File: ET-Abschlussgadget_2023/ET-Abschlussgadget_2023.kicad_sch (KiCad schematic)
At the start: 12 parts, among them U1 ATtiny10-TS

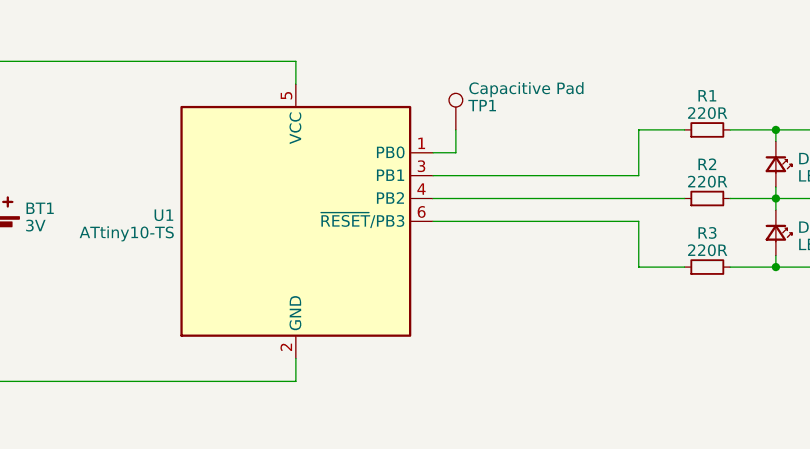
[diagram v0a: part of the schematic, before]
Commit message: Add basic layout
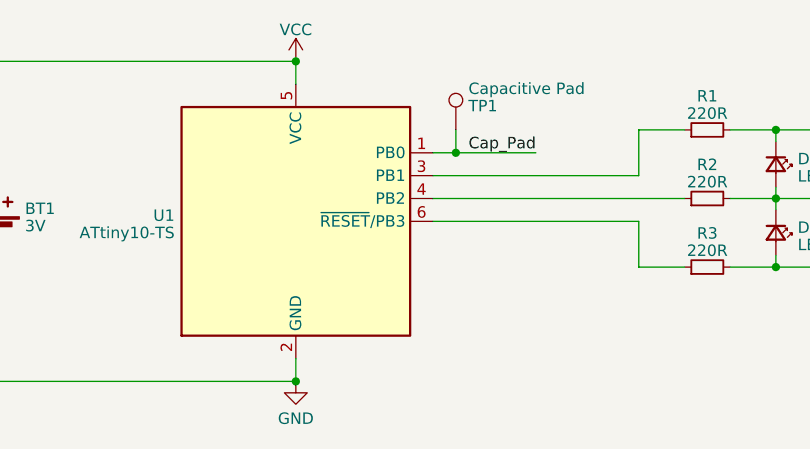
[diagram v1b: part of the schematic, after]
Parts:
- BT1: footprint (none) -> Battery:BatteryHolder_Keystone_3000_1x12mm
- D1, D2, D3, D4, D5: footprint (none) -> LED_SMD:LED_0805_2012Metric_Pad1.15x1.40mm_HandSolder
- D6: footprint (none) -> LED_SMD:LED_LiteOn_LTST-S326
- R1, R2, R3: footprint (none) -> Resistor_SMD:R_0805_2012Metric_Pad1.20x1.40mm_HandSolder
- TP1: footprint (none) -> TestPoint:TestPoint_Pad_4.0x4.0mm
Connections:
- net Cap_Pad: now reaches TP1.1, U1.1 (PB0)
- net VCC: now reaches BT1.1 (+), U1.5 (VCC)
- net GND: now reaches BT1.2 (-), U1.2 (GND)
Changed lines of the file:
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@@
 (kicad_sch (version 20230121) (generator eeschema)
   (paper "A4")
+  (junction (at 106.68 81.28) (diameter 0) (color 0 0 0 0)
+  )
   (junction (at 156.21 93.98) (diameter 0) (color 0 0 0 0)
   )
@@
   (junction (at 142.24 93.98) (diameter 0) (color 0 0 0 0)
   )
+  (junction (at 88.9 106.68) (diameter 0) (color 0 0 0 0)
+  )
   (junction (at 170.18 93.98) (diameter 0) (color 0 0 0 0)
   )
+  (junction (at 88.9 71.12) (diameter 0) (color 0 0 0 0)
+  )
   (junction (at 142.24 78.74) (diameter 0) (color 0 0 0 0)
   )
@@
     (stroke (width 0) (type default))
   )
+  (wire (pts (xy 106.68 81.28) (xy 115.57 81.28))
+    (stroke (width 0) (type default))
+  )
   (wire (pts (xy 106.68 81.28) (xy 104.14 81.28))
     (stroke (width 0) (type default))
@@
     (stroke (width 0) (type default))
   )
+  (label "Cap_Pad" (at 115.57 81.28 180) (fields_autoplaced)
+    (effects (font (size 1.27 1.27)) (justify right bottom))
+  )
   (symbol (lib_id "Device:LED_Small") (at 142.24 82.55 270) (unit 1)
     (in_bom yes) (on_board yes) (dnp no) (fields_autoplaced)
@@
       (effects (font (size 1.27 1.27)) (justify left))
     )
-    (property "Footprint" "" (at 142.24 82.55 90)
+    (property "Footprint" "LED_SMD:LED_0805_2012Metric_Pad1.15x1.40mm_HandSolder" (at 142.24 82.55 90)
       (effects (font (size 1.27 1.27)) hide)
     )
@@
     )
   )
+  (symbol (lib_id "power:GND") (at 88.9 106.68 0) (unit 1)
+    (in_bom yes) (on_board yes) (dnp no) (fields_autoplaced)
+    (property "Reference" "#PWR02" (at 88.9 113.03 0)
+      (effects (font (size 1.27 1.27)) hide)
+    )
+    (property "Value" "GND" (at 88.9 110.8155 0)
+      (effects (font (size 1.27 1.27)))
+    )
+    (property "Footprint" "" (at 88.9 106.68 0)
+      (effects (font (size 1.27 1.27)) hide)
+    )
+    (property "Datasheet" "" (at 88.9 106.68 0)
+      (effects (font (size 1.27 1.27)) hide)
+    )
+    (pin "1")
+    (instances
+      (project "ET-Abschlussgadget_2023"
+        (path "/175a65ba-6b59-4269-bd86-2662d331b61e"
+          (reference "#PWR02") (unit 1)
+        )
+      )
+    )
+  )
   (symbol (lib_id "Device:R_Small") (at 134.62 93.98 90) (unit 1)
     (in_bom yes) (on_board yes) (dnp no) (fields_autoplaced)
@@
       (effects (font (size 1.27 1.27)))
     )
-    (property "Footprint" "" (at 134.62 93.98 0)
+    (property "Footprint" "Resistor_SMD:R_0805_2012Metric_Pad1.20x1.40mm_HandSolder" (at 134.62 93.98 0)
       (effects (font (size 1.27 1.27)) hide)
     )
@@
       (effects (font (size 1.27 1.27)) (justify right))
     )
-    (property "Footprint" "" (at 101.6 78.74 0)
+    (property "Footprint" "TestPoint:TestPoint_Pad_4.0x4.0mm" (at 101.6 78.74 0)
       (effects (font (size 1.27 1.27)) hide)
     )
@@
       (effects (font (size 1.27 1.27)) (justify left))
     )
-    (property "Footprint" "" (at 55.88 88.646 90)
+    (property "Footprint" "Battery:BatteryHolder_Keystone_3000_1x12mm" (at 55.88 88.646 90)
       (effects (font (size 1.27 1.27)) hide)
     )
@@
       (effects (font (size 1.27 1.27)) (justify right))
     )
-    (property "Footprint" "" (at 156.21 82.55 90)
+    (property "Footprint" "LED_SMD:LED_0805_2012Metric_Pad1.15x1.40mm_HandSolder" (at 156.21 82.55 90)
       (effects (font (size 1.27 1.27)) hide)
     )
@@
     )
   )
+  (symbol (lib_id "power:VCC") (at 88.9 71.12 0) (unit 1)
+    (in_bom yes) (on_board yes) (dnp no) (fields_autoplaced)
+    (property "Reference" "#PWR01" (at 88.9 74.93 0)
+      (effects (font (size 1.27 1.27)) hide)
+    )
+    (property "Value" "VCC" (at 88.9 67.6181 0)
+      (effects (font (size 1.27 1.27)))
+    )
+    (property "Footprint" "" (at 88.9 71.12 0)
+      (effects (font (size 1.27 1.27)) hide)
+    )
+    (property "Datasheet" "" (at 88.9 71.12 0)
+      (effects (font (size 1.27 1.27)) hide)
+    )
+    (pin "1")
+    (instances
+      (project "ET-Abschlussgadget_2023"
+        (path "/175a65ba-6b59-4269-bd86-2662d331b61e"
+          (reference "#PWR01") (unit 1)
+        )
+      )
+    )
+  )
   (symbol (lib_id "Device:LED_Small") (at 170.18 86.36 90) (unit 1)
     (in_bom yes) (on_board yes) (dnp no) (fields_autoplaced)
@@
       (effects (font (size 1.27 1.27)) (justify right))
     )
-    (property "Footprint" "" (at 170.18 86.36 90)
+    (property "Footprint" "LED_SMD:LED_0805_2012Metric_Pad1.15x1.40mm_HandSolder" (at 170.18 86.36 90)
       (effects (font (size 1.27 1.27)) hide)
     )
@@
       (effects (font (size 1.27 1.27)) (justify left))
     )
-    (property "Footprint" "" (at 182.88 86.36 90)
+    (property "Footprint" "LED_SMD:LED_LiteOn_LTST-S326" (at 182.88 86.36 90)
       (effects (font (size 1.27 1.27)) hide)
     )
@@
       (effects (font (size 1.27 1.27)) (justify left))
     )
-    (property "Footprint" "" (at 142.24 90.17 90)
+    (property "Footprint" "LED_SMD:LED_0805_2012Metric_Pad1.15x1.40mm_HandSolder" (at 142.24 90.17 90)
       (effects (font (size 1.27 1.27)) hide)
     )
@@
       (effects (font (size 1.27 1.27)))
     )
-    (property "Footprint" "" (at 134.62 86.36 0)
+    (property "Footprint" "Resistor_SMD:R_0805_2012Metric_Pad1.20x1.40mm_HandSolder" (at 134.62 86.36 0)
       (effects (font (size 1.27 1.27)) hide)
     )
@@
       (effects (font (size 1.27 1.27)) (justify right))
     )
-    (property "Footprint" "" (at 156.21 90.17 90)
+    (property "Footprint" "LED_SMD:LED_0805_2012Metric_Pad1.15x1.40mm_HandSolder" (at 156.21 90.17 90)
       (effects (font (size 1.27 1.27)) hide)
     )
@@
       (effects (font (size 1.27 1.27)))
     )
-    (property "Footprint" "" (at 134.62 78.74 0)
-      (effects (font (size 1.27 1.27)) hide)
-    )
+    (property "Footprint" "Resistor_SMD:R_0805_2012Metric_Pad1.20x1.40mm_HandSolder" (at 134.62 78.74 0)
+      (effects (font (size 1.27 1.27)) hide)
+    )

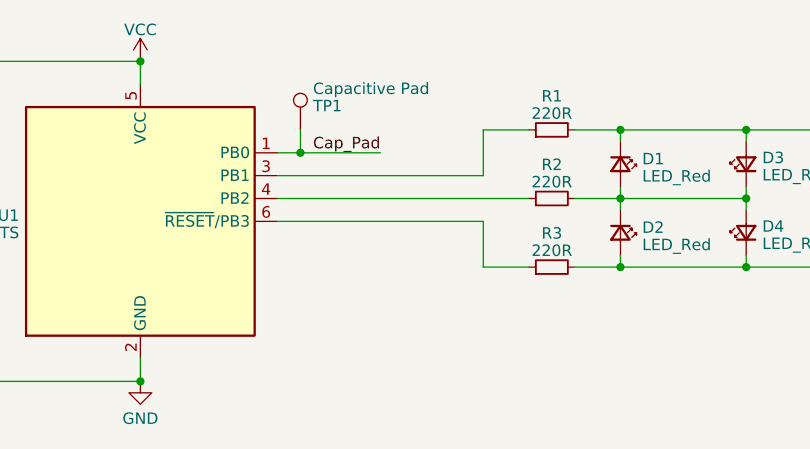
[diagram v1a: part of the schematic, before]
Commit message: Add testpoints, bottom silkscreen, rothli
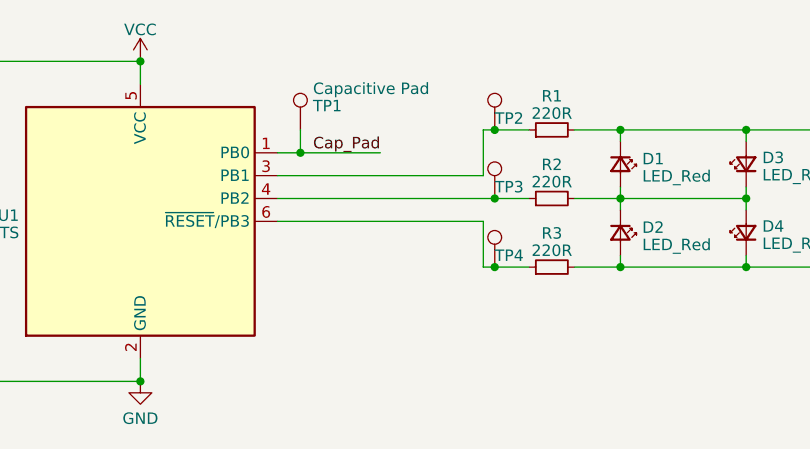
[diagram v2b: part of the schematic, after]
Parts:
- added TP2, TP3, TP4: TestPoint, TestPoint:TestPoint_Pad_1.0x1.0mm, symbol Connector:TestPoint
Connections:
- net at R3.1, U1.6 (~{RESET}/PB3): now also TP4.1
- net at R2.1, U1.4 (PB2): now also TP3.1
- net at R1.1, U1.3 (PB1): now also TP2.1
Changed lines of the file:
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@@
   (junction (at 156.21 93.98) (diameter 0) (color 0 0 0 0)
   )
+  (junction (at 128.27 93.98) (diameter 0) (color 0 0 0 0)
+  )
   (junction (at 170.18 78.74) (diameter 0) (color 0 0 0 0)
   )
@@
   (junction (at 88.9 106.68) (diameter 0) (color 0 0 0 0)
   )
+  (junction (at 128.27 78.74) (diameter 0) (color 0 0 0 0)
+  )
   (junction (at 170.18 93.98) (diameter 0) (color 0 0 0 0)
   )
@@
   (junction (at 156.21 78.74) (diameter 0) (color 0 0 0 0)
   )
+  (junction (at 128.27 86.36) (diameter 0) (color 0 0 0 0)
+  )
   (wire (pts (xy 55.88 85.09) (xy 55.88 71.12))
     (stroke (width 0) (type default))
   )
-  (wire (pts (xy 127 93.98) (xy 132.08 93.98))
+  (wire (pts (xy 128.27 93.98) (xy 132.08 93.98))
+    (stroke (width 0) (type default))
+  )
+  (wire (pts (xy 127 93.98) (xy 128.27 93.98))
     (stroke (width 0) (type default))
   )
@@
     (stroke (width 0) (type default))
   )
-  (wire (pts (xy 104.14 86.36) (xy 132.08 86.36))
+  (wire (pts (xy 104.14 86.36) (xy 128.27 86.36))
     (stroke (width 0) (type default))
   )
@@
     (stroke (width 0) (type default))
   )
-  (wire (pts (xy 127 78.74) (xy 132.08 78.74))
+  (wire (pts (xy 127 78.74) (xy 128.27 78.74))
     (stroke (width 0) (type default))
   )
@@
     (stroke (width 0) (type default))
   )
+  (wire (pts (xy 128.27 86.36) (xy 132.08 86.36))
+    (stroke (width 0) (type default))
+  )
   (wire (pts (xy 142.24 93.98) (xy 137.16 93.98))
     (stroke (width 0) (type default))
@@
   )
   (wire (pts (xy 55.88 106.68) (xy 55.88 92.71))
+    (stroke (width 0) (type default))
+  )
+  (wire (pts (xy 128.27 78.74) (xy 132.08 78.74))
     (stroke (width 0) (type default))
   )
@@
     )
   )
+  (symbol (lib_id "Connector:TestPoint") (at 128.27 86.36 0) (unit 1)
+    (in_bom yes) (on_board yes) (dnp no)
+    (property "Reference" "TP3" (at 128.27 85.09 0)
+      (effects (font (size 1.27 1.27)) (justify left))
+    )
+    (property "Value" "TestPoint" (at 130.81 84.963 0)
+      (effects (font (size 1.27 1.27)) (justify left) hide)
+    )
+    (property "Footprint" "TestPoint:TestPoint_Pad_1.0x1.0mm" (at 133.35 86.36 0)
+      (effects (font (size 1.27 1.27)) hide)
+    )
+    (property "Datasheet" "~" (at 133.35 86.36 0)
+      (effects (font (size 1.27 1.27)) hide)
+    )
+    (pin "1")
+    (instances
+      (project "ET-Abschlussgadget_2023"
+        (path "/175a65ba-6b59-4269-bd86-2662d331b61e"
+          (reference "TP3") (unit 1)
+        )
+      )
+    )
+  )
   (symbol (lib_id "power:VCC") (at 88.9 71.12 0) (unit 1)
     (in_bom yes) (on_board yes) (dnp no) (fields_autoplaced)
@@
     )
   )
+  (symbol (lib_id "Connector:TestPoint") (at 128.27 93.98 0) (unit 1)
+    (in_bom yes) (on_board yes) (dnp no)
+    (property "Reference" "TP4" (at 128.27 92.71 0)
+      (effects (font (size 1.27 1.27)) (justify left))
+    )
+    (property "Value" "TestPoint" (at 130.81 92.583 0)
+      (effects (font (size 1.27 1.27)) (justify left) hide)
+    )
+    (property "Footprint" "TestPoint:TestPoint_Pad_1.0x1.0mm" (at 133.35 93.98 0)
+      (effects (font (size 1.27 1.27)) hide)
+    )
+    (property "Datasheet" "~" (at 133.35 93.98 0)
+      (effects (font (size 1.27 1.27)) hide)
+    )
+    (pin "1")
+    (instances
+      (project "ET-Abschlussgadget_2023"
+        (path "/175a65ba-6b59-4269-bd86-2662d331b61e"
+          (reference "TP4") (unit 1)
+        )
+      )
+    )
+  )
   (symbol (lib_id "Device:LED_Small") (at 170.18 86.36 90) (unit 1)
     (in_bom yes) (on_board yes) (dnp no) (fields_autoplaced)
@@
         )
       )
+    )
+  )
+  (symbol (lib_id "Connector:TestPoint") (at 128.27 78.74 0) (unit 1)
+    (in_bom yes) (on_board yes) (dnp no)
+    (property "Reference" "TP2" (at 128.27 77.47 0)
+      (effects (font (size 1.27 1.27)) (justify left))
+    )
+    (property "Value" "TestPoint" (at 130.81 77.343 0)
+      (effects (font (size 1.27 1.27)) (justify left) hide)
+    )
+    (property "Footprint" "TestPoint:TestPoint_Pad_1.0x1.0mm" (at 133.35 78.74 0)
+      (effects (font (size 1.27 1.27)) hide)
+    )
+    (property "Datasheet" "~" (at 133.35 78.74 0)
+      (effects (font (size 1.27 1.27)) hide)
+    )
+    (pin "1")
+    (instances
+      (project "ET-Abschlussgadget_2023"
+        (path "/175a65ba-6b59-4269-bd86-2662d331b61e"
+          (reference "TP2") (unit 1)
+        )
+      )

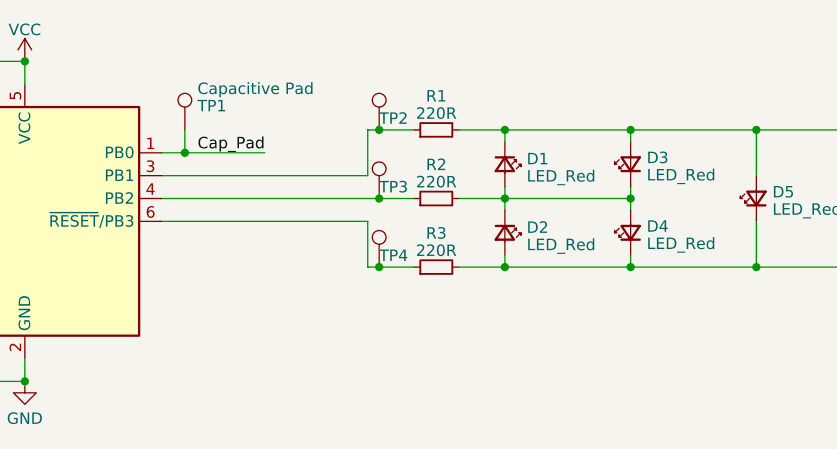
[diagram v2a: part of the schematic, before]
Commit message: Improve component and silkscreen placement
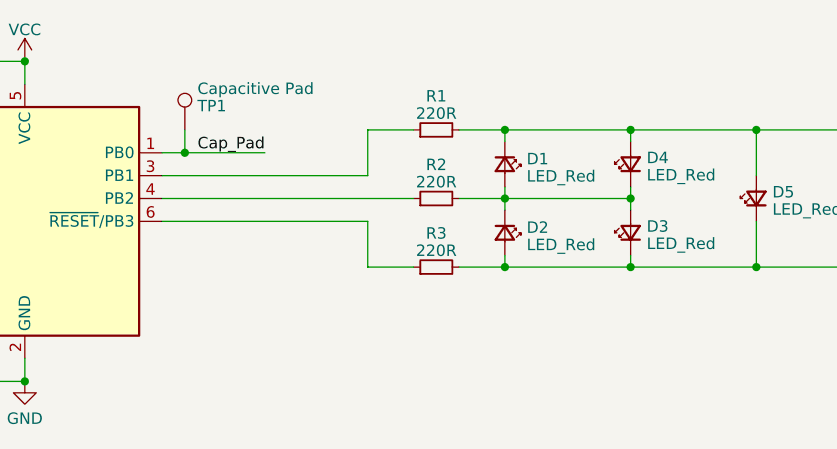
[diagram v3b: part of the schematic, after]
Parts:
- removed TP2, TP3, TP4: TestPoint, TestPoint:TestPoint_Pad_1.0x1.0mm, symbol Connector:TestPoint
- renumbered D4 to D3, D3 to D4

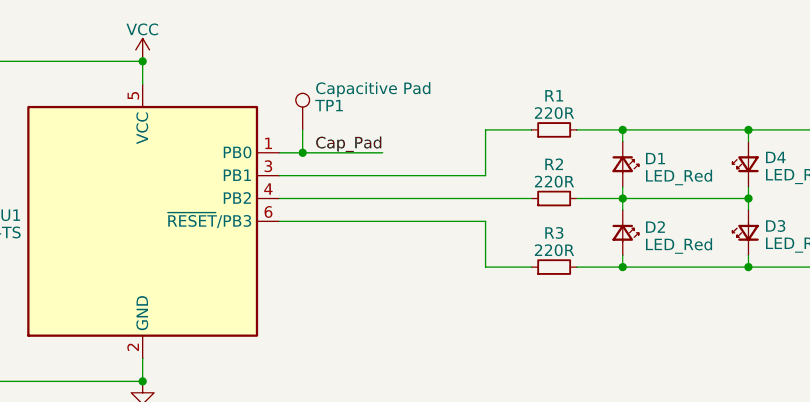
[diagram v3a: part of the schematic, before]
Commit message: Add series resistor to capacitive pad
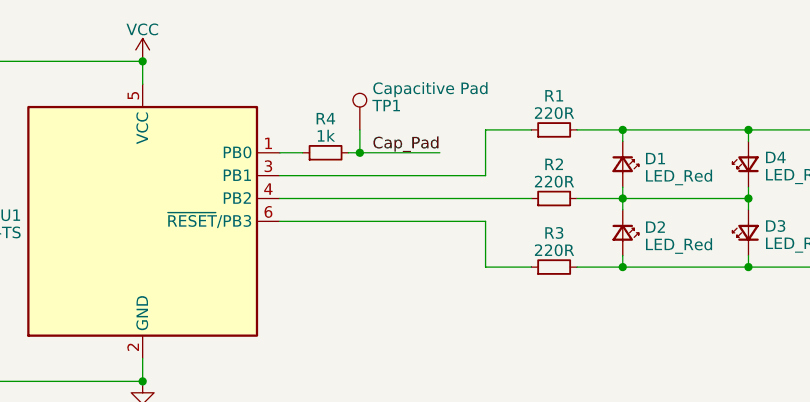
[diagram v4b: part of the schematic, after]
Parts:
- added R4: 1k, Resistor_SMD:R_0805_2012Metric_Pad1.20x1.40mm_HandSolder, symbol Device:R_Small
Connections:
- net Cap_Pad: now also R4.2; no longer U1.1 (PB0)
- new net: R4.1, U1.1 (PB0)
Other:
- moved on the sheet: TP1
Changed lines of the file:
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@@
 (kicad_sch (version 20230121) (generator eeschema)
   (paper "A4")
-  (junction (at 106.68 81.28) (diameter 0) (color 0 0 0 0)
+  (junction (at 113.03 81.28) (diameter 0) (color 0 0 0 0)
   )
   (junction (at 156.21 93.98) (diameter 0) (color 0 0 0 0)
@@
     (stroke (width 0) (type default))
   )
+  (wire (pts (xy 104.14 81.28) (xy 106.68 81.28))
+    (stroke (width 0) (type default))
+  )
   (wire (pts (xy 127 93.98) (xy 132.08 93.98))
     (stroke (width 0) (type default))
@@
     (stroke (width 0) (type default))
   )
-  (wire (pts (xy 106.68 81.28) (xy 115.57 81.28))
-    (stroke (width 0) (type default))
-  )
-  (wire (pts (xy 106.68 81.28) (xy 104.14 81.28))
+  (wire (pts (xy 113.03 81.28) (xy 121.92 81.28))
     (stroke (width 0) (type default))
   )
@@
     (stroke (width 0) (type default))
   )
+  (wire (pts (xy 111.76 81.28) (xy 113.03 81.28))
+    (stroke (width 0) (type default))
+  )
   (wire (pts (xy 156.21 92.71) (xy 156.21 93.98))
     (stroke (width 0) (type default))
@@
     (stroke (width 0) (type default))
   )
-  (wire (pts (xy 106.68 78.74) (xy 106.68 81.28))
+  (wire (pts (xy 113.03 78.74) (xy 113.03 81.28))
     (stroke (width 0) (type default))
   )
@@
     (stroke (width 0) (type default))
   )
-  (label "Cap_Pad" (at 115.57 81.28 180) (fields_autoplaced)
+  (label "Cap_Pad" (at 121.92 81.28 180) (fields_autoplaced)
     (effects (font (size 1.27 1.27)) (justify right bottom))
   )
@@
     )
   )
-  (symbol (lib_id "Connector:TestPoint") (at 106.68 78.74 0) (mirror y) (unit 1)
-    (in_bom yes) (on_board yes) (dnp no) (fields_autoplaced)
-    (property "Reference" "TP1" (at 108.077 76.0817 0)
+  (symbol (lib_id "Device:R_Small") (at 109.22 81.28 90) (unit 1)
+    (in_bom yes) (on_board yes) (dnp no) (fields_autoplaced)
+    (property "Reference" "R4" (at 109.22 77.5335 90)
+      (effects (font (size 1.27 1.27)))
+    )
+    (property "Value" "1k" (at 109.22 79.4545 90)
+      (effects (font (size 1.27 1.27)))
+    )
+    (property "Footprint" "Resistor_SMD:R_0805_2012Metric_Pad1.20x1.40mm_HandSolder" (at 109.22 81.28 0)
+      (effects (font (size 1.27 1.27)) hide)
+    )
+    (property "Datasheet" "~" (at 109.22 81.28 0)
+      (effects (font (size 1.27 1.27)) hide)
+    )
+    (pin "1")
+    (pin "2")
+    (instances
+      (project "ET-Abschlussgadget_2023"
+        (path "/175a65ba-6b59-4269-bd86-2662d331b61e"
+          (reference "R4") (unit 1)
+        )
+      )
+    )
+  )
+  (symbol (lib_id "Connector:TestPoint") (at 113.03 78.74 0) (mirror y) (unit 1)
+    (in_bom yes) (on_board yes) (dnp no) (fields_autoplaced)
+    (property "Reference" "TP1" (at 114.427 76.0817 0)
       (effects (font (size 1.27 1.27)) (justify right))
     )
-    (property "Value" "Capacitive Pad" (at 108.077 74.1607 0)
+    (property "Value" "Capacitive Pad" (at 114.427 74.1607 0)
       (effects (font (size 1.27 1.27)) (justify right))
     )
-    (property "Footprint" "TestPoint:TestPoint_Pad_4.0x4.0mm" (at 101.6 78.74 0)
-      (effects (font (size 1.27 1.27)) hide)
-    )
-    (property "Datasheet" "~" (at 101.6 78.74 0)
-      (effects (font (size 1.27 1.27)) hide)
-    )
+    (property "Footprint" "TestPoint:TestPoint_Pad_4.0x4.0mm" (at 107.95 78.74 0)
+      (effects (font (size 1.27 1.27)) hide)
+    )
+    (property "Datasheet" "~" (at 107.95 78.74 0)
+      (effects (font (size 1.27 1.27)) hide)
+    )
